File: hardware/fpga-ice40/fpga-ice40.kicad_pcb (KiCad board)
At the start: 4 copper layers, 53.3 x 70.1 mm, 61 parts, among them J1 MicroSD_Molex_1040310811, J2 ProgHeader_iCE40, J3 ProgHeader_Flash_QSPI, J4 Conn_02x20_Odd_Even, U1 iCE40HX4K-TQ144, U2 IS42S16320F-6TL, U3 W25Q32JVSS, U4 W25Q32JVSS, U5 S25FL256SAGMFI01, U6 S25FL256SAGMFI01

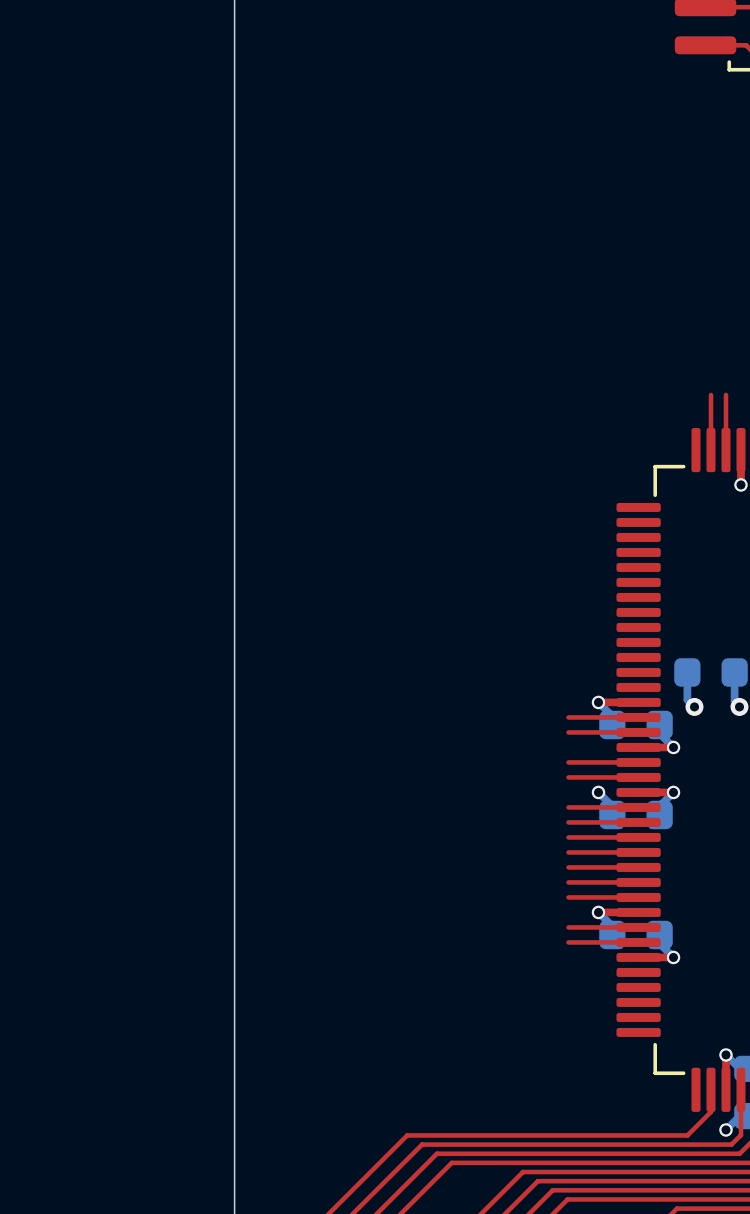
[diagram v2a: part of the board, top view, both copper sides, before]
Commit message: Add FT245RL footprint to layout
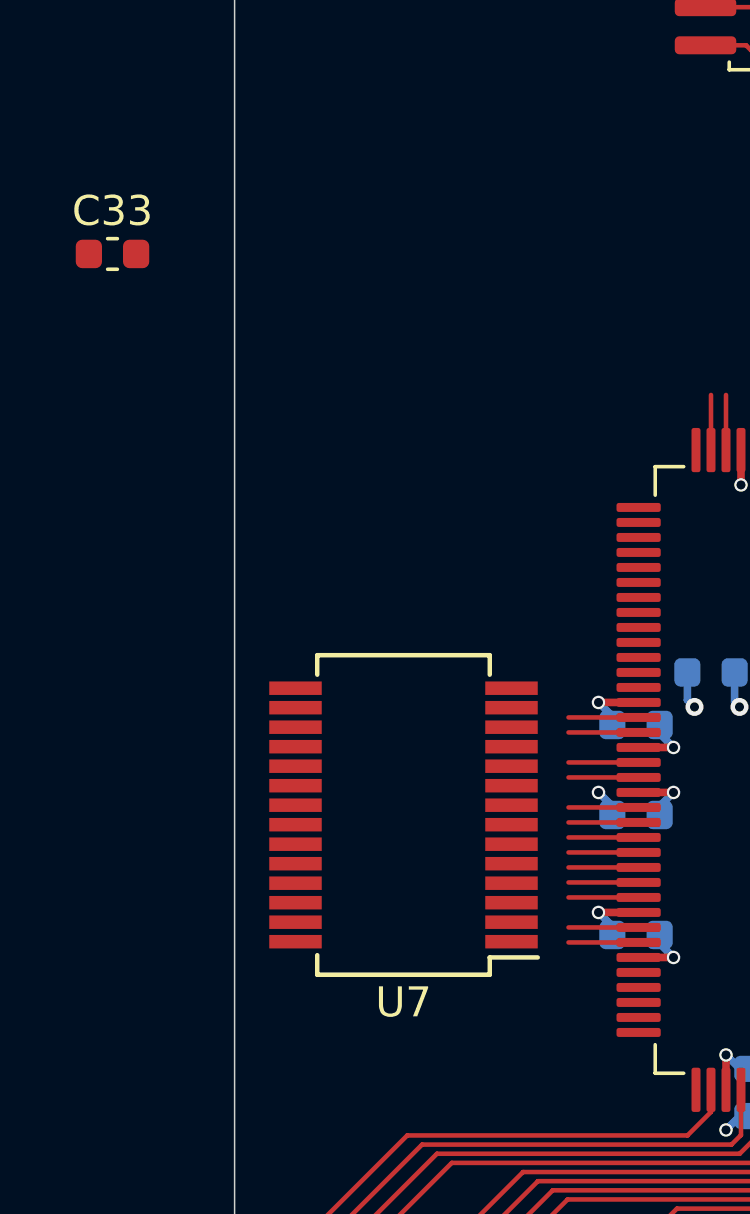
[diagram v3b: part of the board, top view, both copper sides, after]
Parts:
- added C33: 100n, Capacitor_SMD:C_0603_1608Metric, F.Cu at (131.8, 77.8)
- added U7: FT245RL, Package_SO:SSOP-28_5.3x10.2mm_P0.65mm, F.Cu at (141.5, 96.5)
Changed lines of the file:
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@@
     (tracks 637)
     (zones 0)
-    (modules 61)
-    (nets 193)
+    (modules 63)
+    (nets 214)
   )
   (page A4)
@@
   )
   (setup
-    (last_trace_width 0.254)
+    (last_trace_width 0.1524)
     (user_trace_width 0.1524)
     (user_trace_width 0.254)
@@
   (net 191 N64_OS_EVENTn_IC)
   (net 192 "Net-(U1-Pad47)")
+  (net 193 "Net-(U7-Pad28)")
+  (net 194 "Net-(U7-Pad27)")
+  (net 195 "Net-(U7-Pad23)")
+  (net 196 "Net-(U7-Pad22)")
+  (net 197 "Net-(U7-Pad20)")
+  (net 198 "Net-(U7-Pad19)")
+  (net 199 "Net-(C33-Pad1)")
+  (net 200 "Net-(U7-Pad14)")
+  (net 201 "Net-(U7-Pad13)")
+  (net 202 "Net-(U7-Pad12)")
+  (net 203 "Net-(U7-Pad11)")
+  (net 204 "Net-(U7-Pad10)")
+  (net 205 "Net-(U7-Pad9)")
+  (net 206 "Net-(U7-Pad6)")
+  (net 207 "Net-(U7-Pad5)")
+  (net 208 "Net-(U7-Pad4)")
+  (net 209 "Net-(U7-Pad3)")
+  (net 210 "Net-(U7-Pad2)")
+  (net 211 "Net-(U7-Pad1)")
+  (net 212 USB-)
+  (net 213 USB+)
   (net_class Default "This is the default net class."
     (clearance 0.1524)
@@
     (add_net N64_WRITEn)
     (add_net N64_WRITEn_IC)
+    (add_net "Net-(C33-Pad1)")
     (add_net "Net-(J1-Pad9)")
     (add_net "Net-(J4-Pad1)")
@@
     (add_net "Net-(U1-Pad99)")
     (add_net "Net-(U2-Pad40)")
+    (add_net "Net-(U7-Pad1)")
+    (add_net "Net-(U7-Pad10)")
+    (add_net "Net-(U7-Pad11)")
+    (add_net "Net-(U7-Pad12)")
+    (add_net "Net-(U7-Pad13)")
+    (add_net "Net-(U7-Pad14)")
+    (add_net "Net-(U7-Pad19)")
+    (add_net "Net-(U7-Pad2)")
+    (add_net "Net-(U7-Pad20)")
+    (add_net "Net-(U7-Pad22)")
+    (add_net "Net-(U7-Pad23)")
+    (add_net "Net-(U7-Pad27)")
+    (add_net "Net-(U7-Pad28)")
+    (add_net "Net-(U7-Pad3)")
+    (add_net "Net-(U7-Pad4)")
+    (add_net "Net-(U7-Pad5)")
+    (add_net "Net-(U7-Pad6)")
+    (add_net "Net-(U7-Pad9)")
     (add_net P1V2)
     (add_net P3V3)
@@
     (add_net SD_DAT2)
     (add_net SD_DAT3)
+    (add_net USB+)
+    (add_net USB-)
   )
   (net_class FPGA_VCC ""
@@
     (add_net GND)
   )
+  (module Capacitor_SMD:C_0603_1608Metric (layer F.Cu)
+    (at 131.8 77.8)
+    (descr "Capacitor SMD 0603 (1608 Metric), square (rectangular) end terminal, IPC_7351 nominal, (Body size source: http://www.tortai-tech.com/upload/download/2011102023233369053.pdf), generated with kicad-footprint-generator")
+    (tags capacitor)
+    (attr smd)
+    (fp_text reference C33 (at 0 -1.43) (layer F.SilkS)
+      (effects (font (size 1 1) (thickness 0.15)))
+    )
+    (fp_text value 100n (at 0 1.43) (layer F.Fab)
+      (effects (font (size 1 1) (thickness 0.15)))
+    )
+    (fp_text user %R (at 0 0) (layer F.Fab)
+      (effects (font (size 0.4 0.4) (thickness 0.06)))
+    )
+    (fp_line (start 1.48 0.73) (end -1.48 0.73) (layer F.CrtYd) (width 0.05))
+    (fp_line (start 1.48 -0.73) (end 1.48 0.73) (layer F.CrtYd) (width 0.05))
+    (fp_line (start -1.48 -0.73) (end 1.48 -0.73) (layer F.CrtYd) (width 0.05))
+    (fp_line (start -1.48 0.73) (end -1.48 -0.73) (layer F.CrtYd) (width 0.05))
+    (fp_line (start -0.162779 0.51) (end 0.162779 0.51) (layer F.SilkS) (width 0.12))
+    (fp_line (start -0.162779 -0.51) (end 0.162779 -0.51) (layer F.SilkS) (width 0.12))
+    (fp_line (start 0.8 0.4) (end -0.8 0.4) (layer F.Fab) (width 0.1))
+    (fp_line (start 0.8 -0.4) (end 0.8 0.4) (layer F.Fab) (width 0.1))
+    (fp_line (start -0.8 -0.4) (end 0.8 -0.4) (layer F.Fab) (width 0.1))
+    (fp_line (start -0.8 0.4) (end -0.8 -0.4) (layer F.Fab) (width 0.1))
+    (pad 2 smd roundrect (at 0.7875 0) (size 0.875 0.95) (layers F.Cu F.Paste F.Mask) (roundrect_rratio 0.25)
+      (net 54 GND))
+    (pad 1 smd roundrect (at -0.7875 0) (size 0.875 0.95) (layers F.Cu F.Paste F.Mask) (roundrect_rratio 0.25)
+      (net 199 "Net-(C33-Pad1)"))
+    (model ${KISYS3DMOD}/Capacitor_SMD.3dshapes/C_0603_1608Metric.wrl
+      (at (xyz 0 0 0))
+      (scale (xyz 1 1 1))
+      (rotate (xyz 0 0 0))
+    )
+  )
+  (module Package_SO:SSOP-28_5.3x10.2mm_P0.65mm (layer F.Cu)
+    (at 141.5 96.5 180)
+    (descr "28-Lead Plastic Shrink Small Outline (SS)-5.30 mm Body [SSOP] (see Microchip Packaging Specification 00000049BS.pdf)")
+    (tags "SSOP 0.65")
+    (attr smd)
+    (fp_text reference U7 (at 0 -6.25) (layer F.SilkS)
+      (effects (font (size 1 1) (thickness 0.15)))
+    )
+    (fp_text value FT245RL (at 0 6.25) (layer F.Fab)
+      (effects (font (size 1 1) (thickness 0.15)))
+    )
+    (fp_text user %R (at 0 0) (layer F.Fab)
+      (effects (font (size 0.8 0.8) (thickness 0.15)))
+    )
+    (fp_line (start -2.875 -4.75) (end -4.475 -4.75) (layer F.SilkS) (width 0.15))
+    (fp_line (start -2.875 5.325) (end 2.875 5.325) (layer F.SilkS) (width 0.15))
+    (fp_line (start -2.875 -5.325) (end 2.875 -5.325) (layer F.SilkS) (width 0.15))
+    (fp_line (start -2.875 5.325) (end -2.875 4.675) (layer F.SilkS) (width 0.15))
+    (fp_line (start 2.875 5.325) (end 2.875 4.675) (layer F.SilkS) (width 0.15))
+    (fp_line (start 2.875 -5.325) (end 2.875 -4.675) (layer F.SilkS) (width 0.15))
+    (fp_line (start -2.875 -5.325) (end -2.875 -4.75) (layer F.SilkS) (width 0.15))
+    (fp_line (start -4.75 5.5) (end 4.75 5.5) (layer F.CrtYd) (width 0.05))
+    (fp_line (start -4.75 -5.5) (end 4.75 -5.5) (layer F.CrtYd) (width 0.05))
+    (fp_line (start 4.75 -5.5) (end 4.75 5.5) (layer F.CrtYd) (width 0.05))
+    (fp_line (start -4.75 -5.5) (end -4.75 5.5) (layer F.CrtYd) (width 0.05))
+    (fp_line (start -2.65 -4.1) (end -1.65 -5.1) (layer F.Fab) (width 0.15))
+    (fp_line (start -2.65 5.1) (end -2.65 -4.1) (layer F.Fab) (width 0.15))
+    (fp_line (start 2.65 5.1) (end -2.65 5.1) (layer F.Fab) (width 0.15))
+    (fp_line (start 2.65 -5.1) (end 2.65 5.1) (layer F.Fab) (width 0.15))
+    (fp_line (start -1.65 -5.1) (end 2.65 -5.1) (layer F.Fab) (width 0.15))
+    (pad 28 smd rect (at 3.6 -4.225 180) (size 1.75 0.45) (layers F.Cu F.Paste F.Mask)
+      (net 193 "Net-(U7-Pad28)"))
+    (pad 27 smd rect (at 3.6 -3.575 180) (size 1.75 0.45) (layers F.Cu F.Paste F.Mask)
+      (net 194 "Net-(U7-Pad27)"))
+    (pad 26 smd rect (at 3.6 -2.925 180) (size 1.75 0.45) (layers F.Cu F.Paste F.Mask)
+      (net 54 GND))
+    (pad 25 smd rect (at 3.6 -2.275 180) (size 1.75 0.45) (layers F.Cu F.Paste F.Mask)
+      (net 54 GND))
+    (pad 24 smd rect (at 3.6 -1.625 180) (size 1.75 0.45) (layers F.Cu F.Paste F.Mask))
+    (pad 23 smd rect (at 3.6 -0.975 180) (size 1.75 0.45) (layers F.Cu F.Paste F.Mask)
+      (net 195 "Net-(U7-Pad23)"))
+    (pad 22 smd rect (at 3.6 -0.325 180) (size 1.75 0.45) (layers F.Cu F.Paste F.Mask)
+      (net 196 "Net-(U7-Pad22)"))
+    (pad 21 smd rect (at 3.6 0.325 180) (size 1.75 0.45) (layers F.Cu F.Paste F.Mask)
+      (net 54 GND))
+    (pad 20 smd rect (at 3.6 0.975 180) (size 1.75 0.45) (layers F.Cu F.Paste F.Mask)
+      (net 197 "Net-(U7-Pad20)"))
+    (pad 19 smd rect (at 3.6 1.625 180) (size 1.75 0.45) (layers F.Cu F.Paste F.Mask)
+      (net 198 "Net-(U7-Pad19)"))
+    (pad 18 smd rect (at 3.6 2.275 180) (size 1.75 0.45) (layers F.Cu F.Paste F.Mask)
+      (net 54 GND))
+    (pad 17 smd rect (at 3.6 2.925 180) (size 1.75 0.45) (layers F.Cu F.Paste F.Mask)
+      (net 199 "Net-(C33-Pad1)"))
+    (pad 16 smd rect (at 3.6 3.575 180) (size 1.75 0.45) (layers F.Cu F.Paste F.Mask)
+      (net 212 USB-))
+    (pad 15 smd rect (at 3.6 4.225 180) (size 1.75 0.45) (layers F.Cu F.Paste F.Mask)
+      (net 213 USB+))
+    (pad 14 smd rect (at -3.6 4.225 180) (size 1.75 0.45) (layers F.Cu F.Paste F.Mask)
+      (net 200 "Net-(U7-Pad14)"))
+    (pad 13 smd rect (at -3.6 3.575 180) (size 1.75 0.45) (layers F.Cu F.Paste F.Mask)
+      (net 201 "Net-(U7-Pad13)"))
+    (pad 12 smd rect (at -3.6 2.925 180) (size 1.75 0.45) (layers F.Cu F.Paste F.Mask)
+      (net 202 "Net-(U7-Pad12)"))
+    (pad 11 smd rect (at -3.6 2.275 180) (size 1.75 0.45) (layers F.Cu F.Paste F.Mask)
+      (net 203 "Net-(U7-Pad11)"))
+    (pad 10 smd rect (at -3.6 1.625 180) (size 1.75 0.45) (layers F.Cu F.Paste F.Mask)
+      (net 204 "Net-(U7-Pad10)"))
+    (pad 9 smd rect (at -3.6 0.975 180) (size 1.75 0.45) (layers F.Cu F.Paste F.Mask)
+      (net 205 "Net-(U7-Pad9)"))
+    (pad 8 smd rect (at -3.6 0.325 180) (size 1.75 0.45) (layers F.Cu F.Paste F.Mask))
+    (pad 7 smd rect (at -3.6 -0.325 180) (size 1.75 0.45) (layers F.Cu F.Paste F.Mask)
+      (net 54 GND))
+    (pad 6 smd rect (at -3.6 -0.975 180) (size 1.75 0.45) (layers F.Cu F.Paste F.Mask)
+      (net 206 "Net-(U7-Pad6)"))
+    (pad 5 smd rect (at -3.6 -1.625 180) (size 1.75 0.45) (layers F.Cu F.Paste F.Mask)
+      (net 207 "Net-(U7-Pad5)"))
+    (pad 4 smd rect (at -3.6 -2.275 180) (size 1.75 0.45) (layers F.Cu F.Paste F.Mask)
+      (net 208 "Net-(U7-Pad4)"))
+    (pad 3 smd rect (at -3.6 -2.925 180) (size 1.75 0.45) (layers F.Cu F.Paste F.Mask)
+      (net 209 "Net-(U7-Pad3)"))
+    (pad 2 smd rect (at -3.6 -3.575 180) (size 1.75 0.45) (layers F.Cu F.Paste F.Mask)
+      (net 210 "Net-(U7-Pad2)"))
+    (pad 1 smd rect (at -3.6 -4.225 180) (size 1.75 0.45) (layers F.Cu F.Paste F.Mask)
+      (net 211 "Net-(U7-Pad1)"))
+    (model ${KISYS3DMOD}/Package_SO.3dshapes/SSOP-28_5.3x10.2mm_P0.65mm.wrl
+      (at (xyz 0 0 0))
+      (scale (xyz 1 1 1))
+      (rotate (xyz 0 0 0))
+    )
+  )
   (module Resistor_SMD:R_Array_Convex_4x0603 (layer F.Cu)

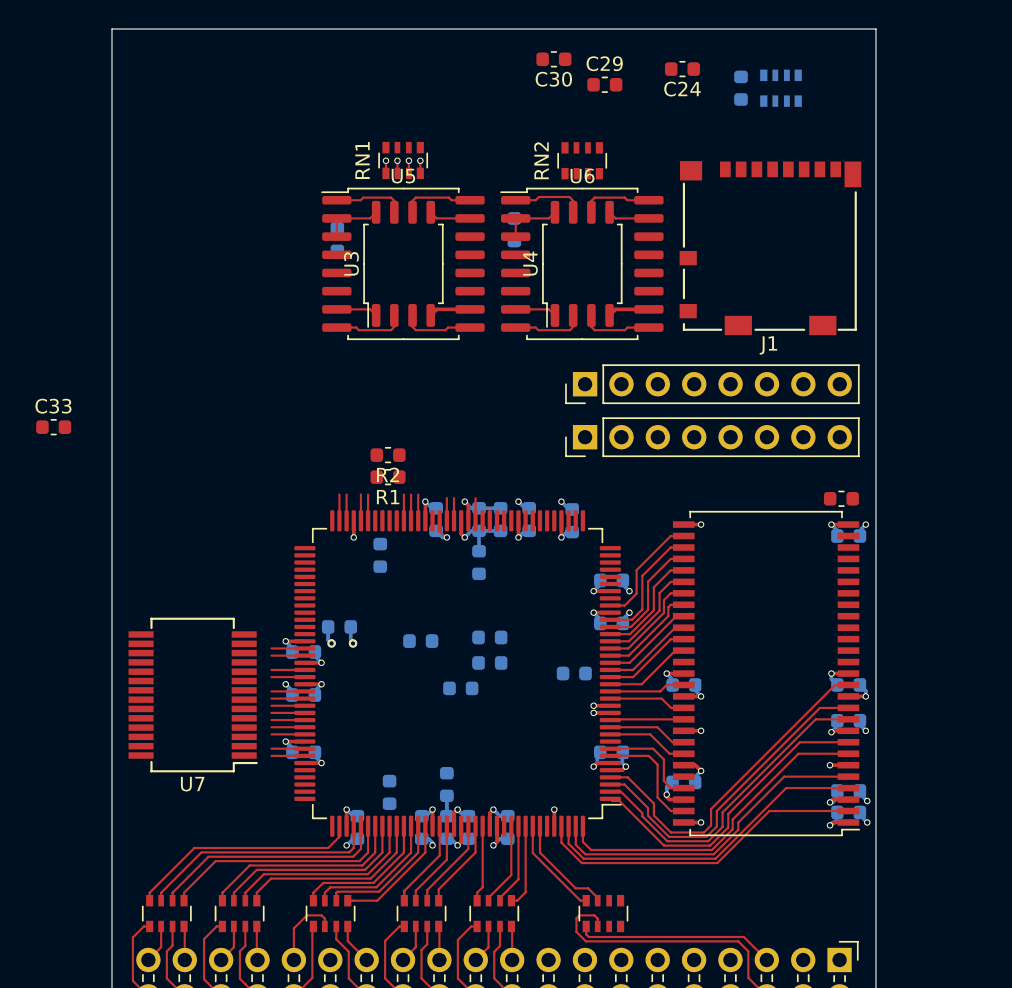
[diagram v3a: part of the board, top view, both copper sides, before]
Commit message: Routing fpga to memory
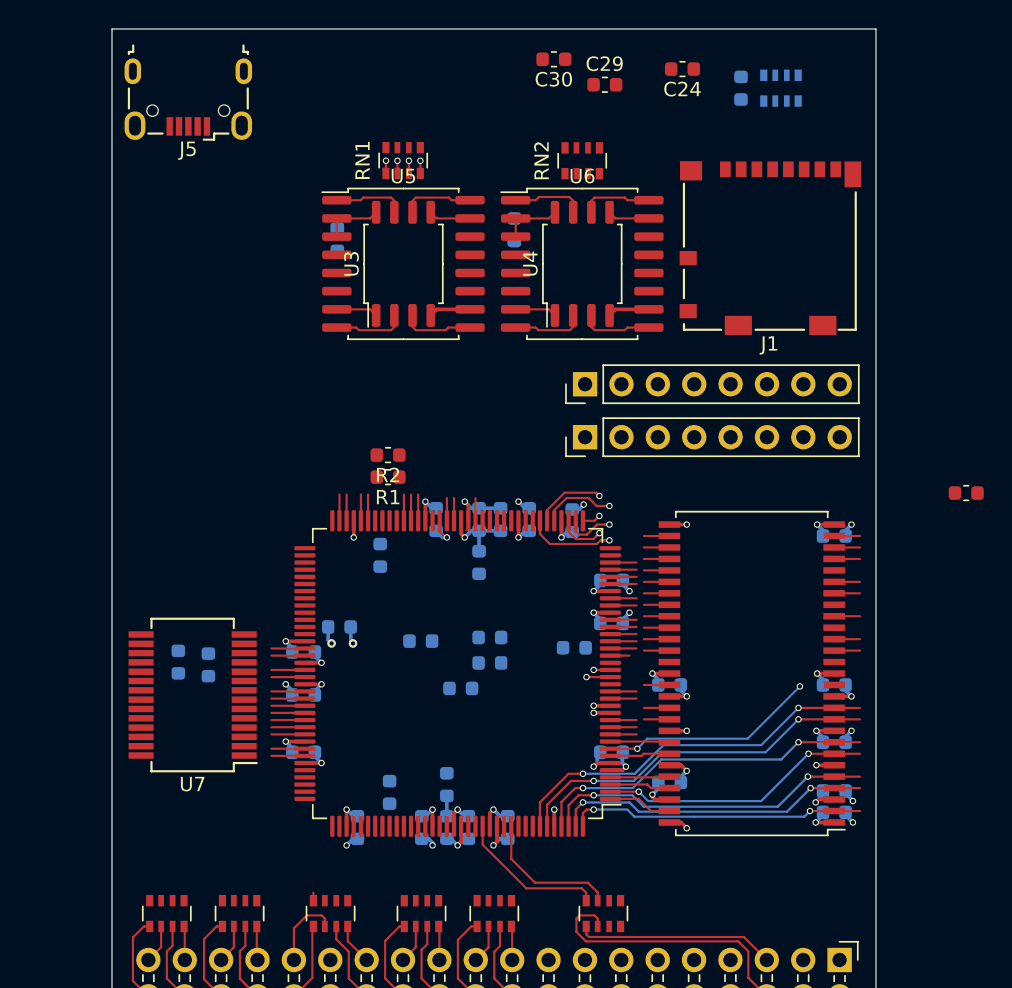
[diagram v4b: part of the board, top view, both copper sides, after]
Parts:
- added J5: USB_B_Micro, Connector_USB:USB_Micro-B_Wuerth_629105150521, F.Cu at (141.2, 54.9)
- added R9: 10k, Resistor_SMD:R_0603_1608Metric, B.Cu at (142.6, 94.4)
- C33: moved to B.Cu
- moved C33 18.6 mm to (140.5, 94.2), turned to 270 degrees
- moved C28 8.72 mm to (195.5, 82.4)
- moved C19 1.80 mm to (186.3, 99.8)
- moved R7 1.80 mm to (168.2, 93.2)
- moved C15 1.00 mm to (186.3, 104.7)
- moved C16 1.00 mm to (186.3, 95.8)
- moved C17 1.00 mm to (186.3, 85.4)
- moved C18 1.00 mm to (186.3, 103.2)
- moved C20 1.00 mm to (174.8, 102.6)
- moved C21 1.00 mm to (174.8, 95.8)
- moved U2 1.00 mm to (180.5, 95.0)
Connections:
- net Net-(U7-Pad1) renamed FIFO_D0
- net Net-(U7-Pad10) renamed FIFO_D6
- net Net-(U7-Pad11) renamed FIFO_D3
- net Net-(U7-Pad13) renamed FIFO_RDn
- net Net-(U7-Pad14) renamed FIFO_WR
- net Net-(U7-Pad2) renamed FIFO_D4
- net Net-(U7-Pad22) renamed FIFO_TXEn
- net Net-(U7-Pad23) renamed FIFO_RXFn
- net Net-(U7-Pad3) renamed FIFO_D2
- net Net-(U7-Pad5) renamed FIFO_D1
- net Net-(U7-Pad6) renamed FIFO_D7
- net Net-(U7-Pad9) renamed FIFO_D5
- U1 pad 1: DRAM_DQ4 -> DRAM_DQ15
- U1 pad 10: DRAM_DQ12 -> Net-(U1-Pad10)
- U1 pad 104: Net-(U1-Pad104) -> N64_AD15_IC
- U1 pad 105: Net-(U1-Pad105) -> N64_AD0_IC
- U1 pad 106: Net-(U1-Pad106) -> N64_AD14_IC
- U1 pad 107: Net-(U1-Pad107) -> N64_AD1_IC
- U1 pad 11: DRAM_DQ11 -> Net-(U1-Pad11)
- U1 pad 110: N64_AD15_IC -> N64_AD13_IC
- U1 pad 112: N64_AD0_IC -> N64_AD2_IC
- U1 pad 113: N64_AD14_IC -> N64_AD12_IC
- U1 pad 114: N64_AD1_IC -> N64_AD3_IC
- U1 pad 115: N64_AD13_IC -> N64_WRITEn_IC
- U1 pad 116: N64_AD2_IC -> N64_ALE_L_IC
- U1 pad 117: N64_AD12_IC -> N64_READn_IC
- U1 pad 118: N64_AD3_IC -> N64_ALE_H_IC
- U1 pad 119: N64_WRITEn_IC -> N64_AD11_IC
- U1 pad 12: DRAM_DQ10 -> Net-(U1-Pad12)
- U1 pad 120: N64_ALE_L_IC -> N64_AD4_IC
- U1 pad 121: N64_READn_IC -> N64_AD10_IC
- U1 pad 122: N64_ALE_H_IC -> N64_AD5_IC
- U1 pad 124: N64_AD11_IC -> N64_AD9_IC
- U1 pad 125: N64_AD4_IC -> N64_AD6_IC
- U1 pad 128: N64_AD10_IC -> N64_AD8_IC
- U1 pad 129: N64_AD5_IC -> N64_AD7_IC
- U1 pad 130: N64_AD9_IC -> N64_COLD_RESETn_IC
- U1 pad 134: N64_AD6_IC -> N64_OS_EVENTn_IC
- U1 pad 135: N64_AD8_IC -> Net-(U1-Pad135)
- U1 pad 136: N64_AD7_IC -> Net-(U1-Pad136)
- U1 pad 137: N64_COLD_RESETn_IC -> Net-(U1-Pad137)
- U1 pad 138: N64_OS_EVENTn_IC -> DRAM_DQ6
- U1 pad 139: Net-(U1-Pad139) -> DRAM_DQ5
- U1 pad 141: DRAM_DQ0 -> DRAM_DQ4
- U1 pad 142: DRAM_DQ1 -> DRAM_DQ2
- U1 pad 143: DRAM_DQ2 -> DRAM_DQ1
- U1 pad 144: DRAM_DQ3 -> DRAM_DQ0
- U1 pad 17: DRAM_UDQM -> Net-(U1-Pad17)
- U1 pad 18: DRAM_CLK -> Net-(U1-Pad18)
- U1 pad 19: DRAM_CKE -> Net-(U1-Pad19)
- U1 pad 2: DRAM_DQ5 -> DRAM_DQ3
- U1 pad 20: DRAM_A12 -> Net-(U1-Pad20)
- U1 pad 21: DRAM_A11 -> Net-(U1-Pad21)
- U1 pad 22: DRAM_A9 -> Net-(U1-Pad22)
- U1 pad 23: DRAM_A8 -> Net-(U1-Pad23)
- U1 pad 24: DRAM_A7 -> Net-(U1-Pad24)
- U1 pad 25: DRAM_A6 -> Net-(U1-Pad25)
- U1 pad 26: DRAM_A5 -> Net-(U1-Pad26)
- U1 pad 28: DRAM_A4 -> Net-(U1-Pad28)
- U1 pad 3: DRAM_DQ6 -> DRAM_DQ14
- U1 pad 4: DRAM_DQ7 -> DRAM_DQ13
- U1 pad 7: DRAM_DQ15 -> DRAM_DQ12
- U1 pad 8: DRAM_DQ14 -> Net-(U1-Pad8)
- U1 pad 9: DRAM_DQ13 -> DRAM_DQ11
- U7 pad 15: USB+ -> USB_D+
- U7 pad 16: USB- -> USB_D-
- U7 pad 20: Net-(U7-Pad20) -> USB_VBUS
- U7 pad 4: Net-(U7-Pad4) -> P3V3
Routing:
- net DRAM_DQ7: track 23.6 -> 0.07 mm
- net N64_AD0_IC: track 16.8 -> 0.00 mm
- net N64_AD14_IC: track 16.6 -> 0.00 mm
- net N64_AD1_IC: track 16.4 -> 0.00 mm
- net N64_AD15_IC: track 16.2 -> 0.00 mm
- net Net-(U1-Pad8): track 0.00 -> 15.0 mm, vias 0 -> 2
- net N64_AD13_IC: track 14.2 -> 0.00 mm
- net N64_AD2_IC: track 13.9 -> 0.00 mm
- net N64_AD12_IC: track 13.6 -> 0.00 mm
- net N64_AD3_IC: track 13.3 -> 0.00 mm
- net N64_ALE_L_IC: track 9.57 -> 0.00 mm
- net N64_WRITEn_IC: track 9.87 -> 0.55 mm
- net N64_READn_IC: track 9.27 -> 0.00 mm
- net N64_ALE_H_IC: track 8.65 -> 0.00 mm
- net DRAM_A5: track 8.59 -> 1.79 mm
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- added copper zone on In1(GND).Cu, net GND
